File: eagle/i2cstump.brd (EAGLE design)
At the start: 31.2 x 19 mm, 21 parts, among them IC1 ATTINY85, IC2 REG1117, J1 I2C-5V, J2 I2C-3V3, Q1 220mA/50V/3.5Ω, Q2 220mA/50V/3.5Ω, X1 USBPCB

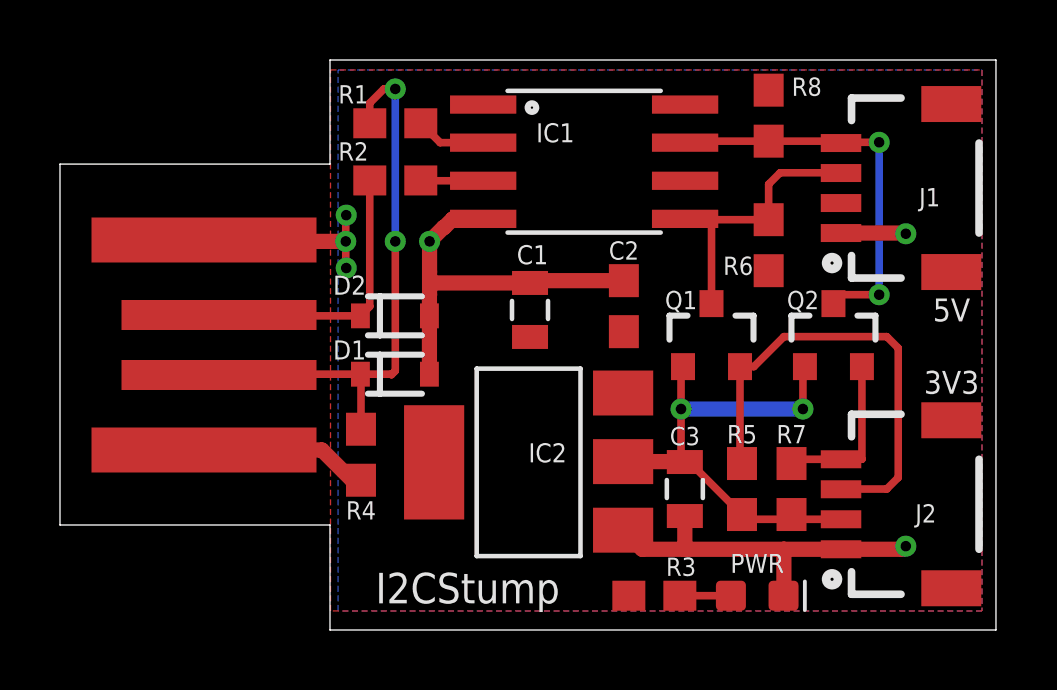
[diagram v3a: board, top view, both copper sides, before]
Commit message: Move AM1117 a bit to the left again, as it was really close to C3
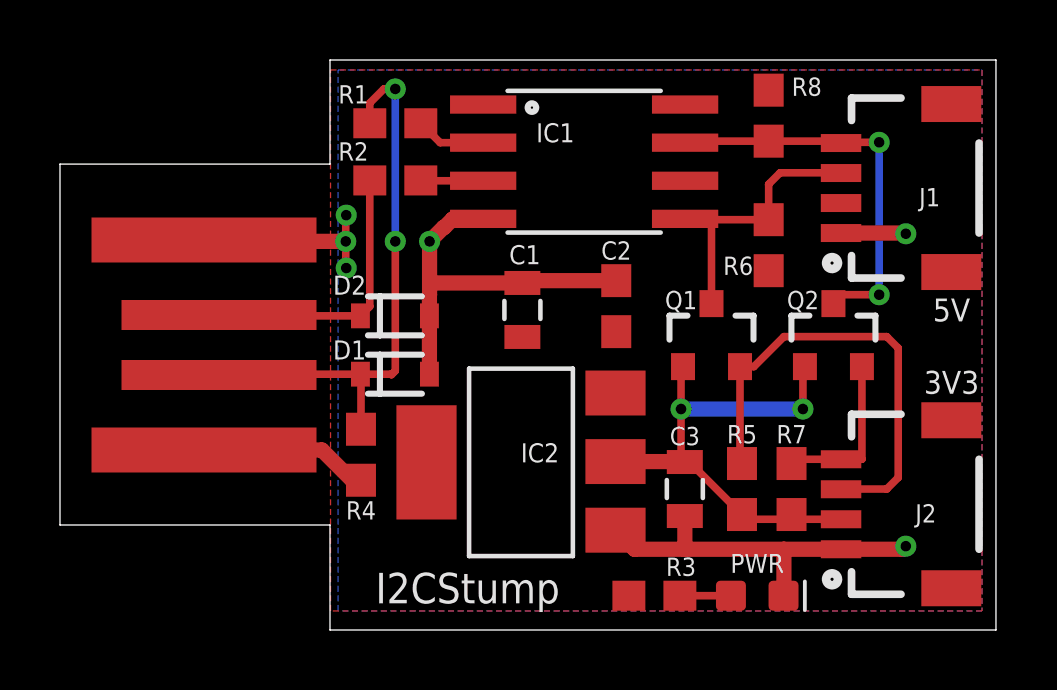
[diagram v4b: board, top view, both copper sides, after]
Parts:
- moved C1 0.25 mm to (15.4, 10.7)
- moved IC2 0.25 mm to (15.4, 5.59)
- moved C2 0.25 mm to (18.5, 10.8)
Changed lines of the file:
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@@
 <wire x1="0" y1="15.53" x2="0" y2="3.5" width="0" layer="20"/>
 <text x="5.6896" y="4.7192" size="1.27" layer="26" font="vector" ratio="18" rot="MR90">Digispark</text>
-<text x="15.748" y="12.827" size="0.635" layer="21" font="vector" ratio="20" distance="80" align="top-center">C1</text>
+<text x="15.494" y="12.827" size="0.635" layer="21" font="vector" ratio="20" distance="80" align="top-center">C1</text>
 <text x="9.652" y="11.811" size="0.635" layer="21" font="vector" ratio="20" distance="80" align="top-center">D2</text>
 <text x="9.652" y="9.652" size="0.635" layer="21" font="vector" ratio="20" distance="80" align="top-center">D1</text>
@@
 <attribute name="VALUE" x="10.1485" y="7.13" size="0.4064" layer="27"/>
 </element>
-<element name="C1" library="SparkFun" package="0805" value="4.7uf" x="15.6674" y="10.668" smashed="yes" rot="R90">
-<attribute name="VALUE" x="17.0644" y="9.652" size="0.4064" layer="27" rot="R90"/>
+<element name="C1" library="SparkFun" package="0805" value="4.7uf" x="15.4134" y="10.668" smashed="yes" rot="R90">
+<attribute name="VALUE" x="16.8104" y="9.652" size="0.4064" layer="27" rot="R90"/>
 </element>
 <element name="J1" library="SparkFun-Connectors" library_urn="urn:adsk.eagle:library:513" package="1X04_1MM_RA" package3d_urn="urn:adsk.eagle:package:38096/1" value="I2C-5V" x="26.035" y="14.732" smashed="yes" rot="R90">
@@
 <attribute name="VALUE" x="29.337" y="13.081" size="0.6096" layer="27" font="vector" ratio="20" rot="R90"/>
 </element>
-<element name="IC2" library="burr-brown" library_urn="urn:adsk.eagle:library:111" package="SOT223" package3d_urn="urn:adsk.eagle:package:4940/1" value="REG1117" x="15.621" y="5.588" smashed="yes" rot="R90">
-<attribute name="MF" value="" x="15.621" y="5.588" size="1.778" layer="27" rot="R90" display="off"/>
-<attribute name="MPN" value="REG1117" x="15.621" y="5.588" size="1.778" layer="27" rot="R90" display="off"/>
-<attribute name="NAME" x="16.891" y="6.223" size="0.635" layer="25" font="vector" ratio="20" rot="R180"/>
-<attribute name="OC_FARNELL" value="1097566" x="15.621" y="5.588" size="1.778" layer="27" rot="R90" display="off"/>
-<attribute name="OC_NEWARK" value="14P6981" x="15.621" y="5.588" size="1.778" layer="27" rot="R90" display="off"/>
-<attribute name="VALUE" x="21.463" y="2.794" size="1.27" layer="27" ratio="10" rot="R90"/>
+<element name="IC2" library="burr-brown" library_urn="urn:adsk.eagle:library:111" package="SOT223" package3d_urn="urn:adsk.eagle:package:4940/1" value="REG1117" x="15.367" y="5.588" smashed="yes" rot="R90">
+<attribute name="MF" value="" x="15.367" y="5.588" size="1.778" layer="27" rot="R90" display="off"/>
+<attribute name="MPN" value="REG1117" x="15.367" y="5.588" size="1.778" layer="27" rot="R90" display="off"/>
+<attribute name="NAME" x="16.637" y="6.223" size="0.635" layer="25" font="vector" ratio="20" rot="R180"/>
+<attribute name="OC_FARNELL" value="1097566" x="15.367" y="5.588" size="1.778" layer="27" rot="R90" display="off"/>
+<attribute name="OC_NEWARK" value="14P6981" x="15.367" y="5.588" size="1.778" layer="27" rot="R90" display="off"/>
+<attribute name="VALUE" x="21.209" y="2.794" size="1.27" layer="27" ratio="10" rot="R90"/>
 </element>
 <element name="J2" library="SparkFun-Connectors" library_urn="urn:adsk.eagle:library:513" package="1X04_1MM_RA" package3d_urn="urn:adsk.eagle:package:38096/1" value="I2C-3V3" x="26.035" y="4.191" smashed="yes" rot="R90">
@@
 <attribute name="VALUE" x="11.176" y="15.748" size="0.6096" layer="27" font="vector" ratio="20" rot="R180" align="top-center"/>
 </element>
-<element name="C2" library="SparkFun-Capacitors" library_urn="urn:adsk.eagle:library:510" package="0603" package3d_urn="urn:adsk.eagle:package:37414/1" value="0.1uF" x="18.796" y="10.795" smashed="yes" rot="R90">
-<attribute name="NAME" x="18.796" y="12.954" size="0.6096" layer="25" font="vector" ratio="20" rot="R180" align="bottom-center"/>
-<attribute name="PROD_ID" value="CAP-00810" x="18.796" y="10.795" size="1.778" layer="27" rot="R90" display="off"/>
-<attribute name="VALUE" x="19.558" y="10.795" size="0.6096" layer="27" font="vector" ratio="20" rot="R90" align="top-center"/>
+<element name="C2" library="SparkFun-Capacitors" library_urn="urn:adsk.eagle:library:510" package="0603" package3d_urn="urn:adsk.eagle:package:37414/1" value="0.1uF" x="18.542" y="10.795" smashed="yes" rot="R90">
+<attribute name="NAME" x="18.542" y="12.954" size="0.6096" layer="25" font="vector" ratio="20" rot="R180" align="bottom-center"/>
+<attribute name="PROD_ID" value="CAP-00810" x="18.542" y="10.795" size="1.778" layer="27" rot="R90" display="off"/>
+<attribute name="VALUE" x="19.304" y="10.795" size="0.6096" layer="27" font="vector" ratio="20" rot="R90" align="top-center"/>
 </element>
 <element name="D3" library="SparkFun-LED" library_urn="urn:adsk.eagle:library:529" package="LED-0603" package3d_urn="urn:adsk.eagle:package:39354/1" value="GREEN" x="23.241" y="1.143" smashed="yes">
@@
 <wire x1="4.846" y1="12.954" x2="9.525" y2="12.954" width="0.508" layer="1"/>
 <via x="9.525" y="12.954" extent="1-16" drill="0.35"/>
-<wire x1="18.796" y1="11.645" x2="18.719" y2="11.568" width="0.254" layer="1"/>
+<wire x1="18.542" y1="11.645" x2="18.465" y2="11.568" width="0.254" layer="1"/>
 <via x="28.194" y="2.794" extent="1-16" drill="0.35"/>
 <via x="28.194" y="13.208" extent="1-16" drill="0.35"/>
@@
 </polygon>
 <contactref element="D3" pad="C"/>
-<wire x1="15.7444" y1="11.645" x2="15.6674" y2="11.568" width="0.508" layer="1"/>
+<wire x1="15.4904" y1="11.645" x2="15.4134" y2="11.568" width="0.508" layer="1"/>
 <wire x1="12.3145" y1="11.1715" x2="12.3145" y2="10.472" width="0.508" layer="1"/>
 <wire x1="12.3145" y1="10.472" x2="12.3145" y2="8.527" width="0.508" layer="1"/>
@@
 <wire x1="12.8074625" y1="13.4192" x2="12.7842" y2="13.4192" width="0.508" layer="1"/>
 <wire x1="12.7842" y1="13.4192" x2="12.319" y2="12.954" width="0.508" layer="1"/>
-<wire x1="12.319" y1="12.954" x2="12.319" y2="11.938" width="0.508" layer="1"/>
-<wire x1="12.319" y1="11.938" x2="12.319" y2="11.684" width="0.508" layer="1"/>
+<wire x1="12.319" y1="12.954" x2="12.319" y2="11.684" width="0.508" layer="1"/>
 <wire x1="12.319" y1="11.684" x2="12.319" y2="11.176" width="0.508" layer="1"/>
 <wire x1="12.319" y1="11.176" x2="12.3145" y2="11.1715" width="0.508" layer="1"/>
-<wire x1="18.796" y1="11.645" x2="15.7444" y2="11.645" width="0.508" layer="1"/>
-<wire x1="15.6674" y1="11.568" x2="12.435" y2="11.568" width="0.508" layer="1"/>
+<wire x1="18.542" y1="11.645" x2="15.4904" y2="11.645" width="0.508" layer="1"/>
+<wire x1="15.4134" y1="11.568" x2="12.435" y2="11.568" width="0.508" layer="1"/>
 <wire x1="12.435" y1="11.568" x2="12.319" y2="11.684" width="0.508" layer="1"/>
 <wire x1="26.035" y1="2.691" x2="24.13" y2="2.691" width="0.508" layer="1"/>
 <wire x1="24.13" y1="2.691" x2="20.828" y2="2.691" width="0.508" layer="1"/>
-<wire x1="20.828" y1="2.691" x2="19.407" y2="2.691" width="0.508" layer="1"/>
-<wire x1="19.407" y1="2.691" x2="18.7706" y2="3.3274" width="0.508" layer="1"/>
+<wire x1="20.828" y1="2.691" x2="19.153" y2="2.691" width="0.508" layer="1"/>
+<wire x1="19.153" y1="2.691" x2="18.5166" y2="3.3274" width="0.508" layer="1"/>
 <wire x1="26.035" y1="2.691" x2="28.091" y2="2.691" width="0.508" layer="1"/>
 <wire x1="28.091" y1="2.691" x2="28.194" y2="2.794" width="0.508" layer="1"/>
@@
 <wire x1="24.384" y1="3.691" x2="24.384" y2="3.849" width="0.254" layer="1"/>
 <wire x1="20.828" y1="5.599" x2="20.8136" y2="5.6134" width="0.508" layer="1"/>
-<wire x1="20.8136" y1="5.6134" x2="18.7706" y2="5.6134" width="0.508" layer="1"/>
+<wire x1="20.8136" y1="5.6134" x2="18.5166" y2="5.6134" width="0.508" layer="1"/>
 <wire x1="20.701" y1="8.713" x2="20.767" y2="8.779" width="0.508" layer="1"/>
 <wire x1="24.765" y1="8.713" x2="24.831" y2="8.779" width="0.508" layer="1"/>

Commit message: Version 2.0
Now with ICSP touchpoints at the bottom so I can flash the AVR.
Also placed tantalum cap C3 (4.uF) on the output of the AM1117.
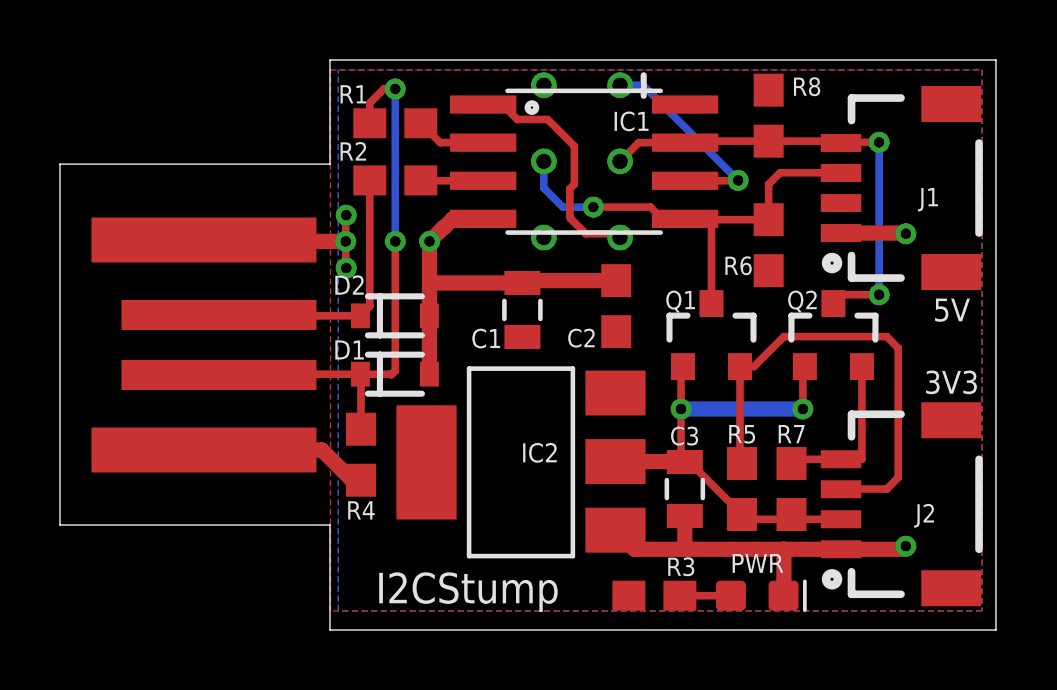
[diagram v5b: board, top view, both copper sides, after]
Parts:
- added J3: AVR_SPI_PROG_3X2TESTPOINTS, SparkFun-Connectors:2X3_TEST_POINTS
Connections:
- new net MISO: IC1.6, J3.1
- new net RST: IC1.1, J3.5
- net 5V: now also J3.2
- net GND: now also J3.6
- net SCL: now also J3.3
- net SDA: now also J3.4
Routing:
- net RST: track 0.00 -> 8.01 mm
- net MISO: track 0.00 -> 7.03 mm, vias 0 -> 1
- net SDA: track 9.38 -> 15.4 mm, vias 0 -> 1
- net SCL: track 13.3 -> 15.7 mm
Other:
- board text added: "CLK"
- board text added: "ICSP"
- board text added: "MISO"
- board text added: "MOSI"
- board text added: "RST"
- board text added: "github.com/pimvanpelt/i2cstump I2C, 3.3V & 5V Version 2.0"
- board text removed: "github.com/pimvanpelt/i2cstump I2C, 3.3V & 5V Version 1.0"
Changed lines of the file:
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@@
 <wire x1="0" y1="15.53" x2="0" y2="3.5" width="0" layer="20"/>
 <text x="5.6896" y="4.7192" size="1.27" layer="26" font="vector" ratio="18" rot="MR90">Digispark</text>
-<text x="15.494" y="12.827" size="0.635" layer="21" font="vector" ratio="20" distance="80" align="top-center">C1</text>
+<text x="14.224" y="10.033" size="0.635" layer="21" font="vector" ratio="20" distance="80" align="top-center">C1</text>
 <text x="9.652" y="11.811" size="0.635" layer="21" font="vector" ratio="20" distance="80" align="top-center">D2</text>
 <text x="9.652" y="9.652" size="0.635" layer="21" font="vector" ratio="20" distance="80" align="top-center">D1</text>
-<text x="16.51" y="16.891" size="0.635" layer="21" font="vector" ratio="20" distance="80" align="top-center">IC1</text>
+<text x="19.05" y="17.272" size="0.635" layer="21" font="vector" ratio="20" distance="80" align="top-center">IC1</text>
 <text x="30.226" y="16.256" size="0.635" layer="22" font="vector" ratio="20" distance="80" rot="MR0" align="center-left">SCL</text>
 <text x="30.226" y="5.715" size="0.635" layer="22" font="vector" ratio="20" distance="80" rot="MR0" align="center-left">SCL</text>
@@
 <text x="30.226" y="3.81" size="0.635" layer="22" font="vector" ratio="20" distance="80" rot="MR0" align="center-left">3v3</text>
 <text x="23.241" y="1.905" size="0.635" layer="21" font="vector" ratio="20" distance="80" align="bottom-center">PWR</text>
-<text x="18.542" y="9.525" size="0.635" layer="22" font="vector" ratio="20" distance="80" rot="MR0" align="center">github.com/pimvanpelt/i2cstump
+<text x="17.78" y="3.937" size="0.635" layer="22" font="vector" ratio="20" distance="80" rot="MR0" align="center">github.com/pimvanpelt/i2cstump
 I2C, 3.3V &amp; 5V
-Version 1.0</text>
+Version 2.0</text>
 <text x="29.718" y="11.049" size="0.762" layer="21" font="vector" ratio="20" rot="R180" align="bottom-center">5V</text>
 <text x="29.718" y="7.874" size="0.762" layer="21" font="vector" ratio="20" rot="R180" align="top-center">3V3</text>
 <text x="13.589" y="1.905" size="1.016" layer="21" font="vector" ratio="20" align="top-center">I2CStump</text>
+<text x="20.066" y="18.161" size="0.762" layer="22" font="vector" ratio="20" rot="MR0" align="center-right">MISO</text>
+<text x="14.859" y="15.621" size="0.762" layer="22" font="vector" ratio="20" rot="MR0" align="center-left">MOSI</text>
+<text x="20.066" y="13.081" size="0.762" layer="22" font="vector" ratio="20" rot="MR0" align="center-right">RST</text>
+<text x="14.859" y="13.081" size="0.762" layer="22" font="vector" ratio="20" rot="MR0" align="center-left">GND</text>
+<text x="20.066" y="15.621" size="0.762" layer="22" font="vector" ratio="20" rot="MR0" align="center-right">CLK</text>
+<text x="14.859" y="18.161" size="0.762" layer="22" font="vector" ratio="20" rot="MR0" align="center-left">5V</text>
+<text x="17.145" y="11.557" size="1.016" layer="22" font="vector" ratio="20" rot="MR0" align="center">ICSP</text>
 </plain>
 <attributes>
@@
 </element>
 <element name="C2" library="SparkFun-Capacitors" library_urn="urn:adsk.eagle:library:510" package="0603" package3d_urn="urn:adsk.eagle:package:37414/1" value="0.1uF" x="18.542" y="10.795" smashed="yes" rot="R90">
-<attribute name="NAME" x="18.542" y="12.954" size="0.6096" layer="25" font="vector" ratio="20" rot="R180" align="bottom-center"/>
+<attribute name="NAME" x="17.399" y="10.033" size="0.6096" layer="25" font="vector" ratio="20" rot="R180" align="bottom-center"/>
 <attribute name="PROD_ID" value="CAP-00810" x="18.542" y="10.795" size="1.778" layer="27" rot="R90" display="off"/>
 <attribute name="VALUE" x="19.304" y="10.795" size="0.6096" layer="27" font="vector" ratio="20" rot="R90" align="top-center"/>
@@
 <attribute name="NAME" x="20.828" y="6.1595" size="0.6096" layer="25" font="vector" ratio="20" align="bottom-center"/>
 <attribute name="VALUE" x="19.431" y="5.715" size="0.4064" layer="27" rot="R270"/>
+</element>
+<element name="J3" library="SparkFun-Connectors" library_urn="urn:adsk.eagle:library:513" package="2X3_TEST_POINTS" package3d_urn="urn:adsk.eagle:package:38008/1" value="AVR_SPI_PROG_3X2TESTPOINTS" x="17.399" y="15.621" smashed="yes" rot="MR270">
+<attribute name="VALUE" x="20.447" y="18.669" size="0.6096" layer="28" font="vector" ratio="20" rot="MR270"/>
 </element>
 </elements>
@@
 <contactref element="X1" pad="GND"/>
 <contactref element="C1" pad="2"/>
-<wire x1="14.1512" y1="13.75" x2="14.1058" y2="13.7046" width="0.3048" layer="1"/>
 <contactref element="J1" pad="1"/>
 <contactref element="IC2" pad="1"/>
@@
 <wire x1="4.846" y1="12.954" x2="9.525" y2="12.954" width="0.508" layer="1"/>
 <via x="9.525" y="12.954" extent="1-16" drill="0.35"/>
-<wire x1="18.542" y1="11.645" x2="18.465" y2="11.568" width="0.254" layer="1"/>
 <via x="28.194" y="2.794" extent="1-16" drill="0.35"/>
 <via x="28.194" y="13.208" extent="1-16" drill="0.35"/>
 <via x="12.319" y="12.954" extent="1-16" drill="0.35"/>
-<wire x1="12.3145" y1="8.527" x2="12.4595" y2="8.382" width="0.254" layer="1"/>
 <polygon width="0.254" layer="16">
 <vertex x="9.271" y="18.669"/>
@@
 <wire x1="9.5396" y1="13.8284" x2="9.5414" y2="13.8284" width="0.254" layer="1"/>
 <via x="9.5414" y="13.8284" extent="1-16" drill="0.35"/>
+<contactref element="J3" pad="6"/>
 </signal>
 <signal name="5V">
@@
 <contactref element="R8" pad="2"/>
 <contactref element="R6" pad="2"/>
+<contactref element="J3" pad="2"/>
 </signal>
 <signal name="N$1">
@@
 <wire x1="23.622" y1="13.677" x2="21.7446" y2="13.677" width="0.254" layer="1"/>
 <wire x1="21.7446" y1="13.677" x2="21.717" y2="13.7046" width="0.254" layer="1"/>
+<contactref element="J3" pad="4"/>
+<wire x1="17.78" y1="14.097" x2="16.764" y2="14.097" width="0.254" layer="16"/>
+<wire x1="16.764" y1="14.097" x2="16.129" y2="14.732" width="0.254" layer="16"/>
+<wire x1="16.129" y1="14.732" x2="16.129" y2="15.621" width="0.254" layer="16"/>
+<via x="17.78" y="14.097" extent="1-16" drill="0.35"/>
+<wire x1="17.78" y1="14.097" x2="19.685" y2="14.097" width="0.254" layer="1"/>
+<wire x1="19.685" y1="14.097" x2="20.0774" y2="13.7046" width="0.254" layer="1"/>
+<wire x1="20.0774" y1="13.7046" x2="20.8368" y2="13.7046" width="0.254" layer="1"/>
 </signal>
 <signal name="N$6">
@@
 <wire x1="23.622" y1="16.295" x2="20.8872" y2="16.295" width="0.254" layer="1"/>
 <wire x1="20.8872" y1="16.295" x2="20.8368" y2="16.2446" width="0.254" layer="1"/>
+<contactref element="J3" pad="3"/>
+<wire x1="20.8368" y1="16.2446" x2="19.2926" y2="16.2446" width="0.254" layer="1"/>
+<wire x1="19.2926" y1="16.2446" x2="18.669" y2="15.621" width="0.254" layer="1"/>
 </signal>
 <signal name="+3V3">
@@
 <wire x1="22.364" y1="1.143" x2="20.662" y2="1.143" width="0.254" layer="1"/>
 </signal>
+<signal name="RST">
+<contactref element="J3" pad="5"/>
+<contactref element="IC1" pad="1"/>
+<wire x1="18.669" y1="13.081" x2="18.542" y2="13.208" width="0.254" layer="1"/>
+<wire x1="17.526" y1="13.208" x2="18.542" y2="13.208" width="0.254" layer="1"/>
+<wire x1="17.526" y1="13.208" x2="17.018" y2="13.716" width="0.254" layer="1"/>
+<wire x1="17.018" y1="13.716" x2="17.018" y2="13.74940625" width="0.254" layer="1"/>
+<wire x1="17.018" y1="13.74940625" x2="16.9954" y2="13.77200625" width="0.254" layer="1"/>
+<wire x1="16.9954" y1="13.77200625" x2="16.9954" y2="14.7094" width="0.254" layer="1"/>
+<wire x1="16.9954" y1="14.7094" x2="17.145" y2="14.859" width="0.254" layer="1"/>
+<wire x1="17.145" y1="16.129" x2="17.145" y2="14.859" width="0.254" layer="1"/>
+<wire x1="16.256" y1="17.018" x2="17.145" y2="16.129" width="0.254" layer="1"/>
+<wire x1="14.1058" y1="17.5146" x2="14.7434" y2="17.5146" width="0.254" layer="1"/>
+<wire x1="15.24" y1="17.018" x2="16.256" y2="17.018" width="0.254" layer="1"/>
+<wire x1="14.7434" y1="17.5146" x2="15.24" y2="17.018" width="0.254" layer="1"/>
+</signal>
+<signal name="MISO">
+<contactref element="J3" pad="1"/>
+<contactref element="IC1" pad="6"/>
+<wire x1="20.8368" y1="14.9746" x2="22.5946" y2="14.9746" width="0.254" layer="1"/>
+<wire x1="22.5946" y1="14.9746" x2="22.606" y2="14.986" width="0.254" layer="1"/>
+<via x="22.606" y="14.986" extent="1-16" drill="0.35"/>
+<wire x1="22.606" y1="14.986" x2="19.431" y2="18.161" width="0.254" layer="16"/>
+<wire x1="19.431" y1="18.161" x2="18.669" y2="18.161" width="0.254" layer="16"/>
+</signal>
 </signals>
